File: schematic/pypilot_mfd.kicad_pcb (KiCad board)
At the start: 2 copper layers, 115.8 x 85 mm, 67 parts, among them J1 usb, J2 keypad, J3 Conn_01x02, J4 Conn_01x02, J5 jlx256160, J6 usb, J7 keypad, Q1 Q_PMOS_GSD, Q2 Q_PMOS_GSD, Q3 Q_PMOS_DSG, SW1 BOOT/AP, U1 CH340G, U2 AMS1117-3.3, U3 ESP32-WROOM-32D, U4 BMP280, U5 ADM2587E, U6 LIS2DE12, Y1 12mhz

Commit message: improvements,  ais plotting working
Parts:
- moved J3 1.20 mm to (151.9, 112.8)
- moved J4 1.20 mm to (61.5, 113.0)
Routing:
- net Net-(J1-Pad1): track 49.2 -> 57.0 mm
- net +5V: track 54.4 -> 59.3 mm, vias 2 -> 3
- net TX: track 91.5 -> 87.2 mm
- net +3V3: track 351.9 -> 352.9 mm
- net GND: track 452.8 -> 452.5 mm, vias 11 -> 12
- added copper zone on F.Cu, net +3V3
- added copper zone on B.Cu, net +5V
- added copper zone on B.Cu, net GND
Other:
- outline, holes or cut-outs redrawn

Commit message: update schematic and code fixes
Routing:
- net GND: track 452.5 -> 454.9 mm
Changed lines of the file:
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@@
   (segment (start 73.425 41.775) (end 73.475 42.4875) (width 0.5) (layer F.Cu) (net 1))
   (segment (start 76.325 40.675) (end 75.55 40.575) (width 0.5) (layer F.Cu) (net 1))
-  (segment (start 64.68 32.445) (end 64.68 34.45) (width 0.8) (layer B.Cu) (net 1))
-  (segment (start 65.1 32.025) (end 64.68 32.445) (width 0.8) (layer B.Cu) (net 1))
-  (segment (start 73.475 32.025) (end 65.1 32.025) (width 0.8) (layer B.Cu) (net 1))
-  (segment (start 76.325 40.675) (end 73.475 32.025) (width 0.8) (layer B.Cu) (net 1))
   (segment (start 75.55 40.575) (end 73.425 41.775) (width 0.5) (layer F.Cu) (net 1))
   (via (at 76.325 40.675) (size 0.8) (drill 0.4) (layers F.Cu B.Cu) (net 1))
@@
   (segment (start 72.375 83.65) (end 72.45 83.575) (width 0.4) (layer F.Cu) (net 1))
   (segment (start 72.375 85.375) (end 72.375 83.65) (width 0.4) (layer F.Cu) (net 1))
-  (segment (start 69.6 99.05) (end 69.575 84.475) (width 0.6) (layer B.Cu) (net 1))
-  (segment (start 74.35 101.55) (end 69.6 99.05) (width 0.6) (layer B.Cu) (net 1))
-  (segment (start 90.35 101.8625) (end 74.35 101.55) (width 0.6) (layer B.Cu) (net 1))
+  (segment (start 69.6 100.75) (end 69.575 84.475) (width 0.6) (layer B.Cu) (net 1))
+  (segment (start 70.25 101.75) (end 69.6 100.75) (width 0.6) (layer B.Cu) (net 1))
+  (segment (start 90.35 101.8625) (end 70.25 101.75) (width 0.6) (layer B.Cu) (net 1))
   (segment (start 92.725 98.4) (end 90.35 101.8625) (width 0.6) (layer B.Cu) (net 1))
+  (segment (start 64.68 32.445) (end 64.68 34.45) (width 0.8) (layer B.Cu) (net 1))
+  (segment (start 65.1 32.025) (end 64.68 32.445) (width 0.8) (layer B.Cu) (net 1))
+  (segment (start 74.55 32.025) (end 65.1 32.025) (width 0.8) (layer B.Cu) (net 1))
+  (segment (start 76.325 40.675) (end 74.55 32.025) (width 0.8) (layer B.Cu) (net 1))
   (segment (start 72.475 87.975) (end 78.775 87.975) (width 0.6) (layer F.Cu) (net 2))
   (segment (start 77.6 81.075) (end 76.975 81.075) (width 0.6) (layer F.Cu) (net 2))
@@
   (segment (start 100.425 61.95) (end 90.68 52.205) (width 0.4) (layer F.Cu) (net 11))
   (via (at 118.95 113) (size 0.8) (drill 0.4) (layers F.Cu B.Cu) (net 11))
-  (segment (start 106.025 67.55) (end 100.425 61.95) (width 0.4) (layer B.Cu) (net 11))
-  (segment (start 119.175 87.175) (end 106.025 74.025) (width 0.4) (layer B.Cu) (net 11))
-  (segment (start 106.025 74.025) (end 106.025 67.55) (width 0.4) (layer B.Cu) (net 11))
-  (segment (start 119.15 98.1) (end 119.175 87.175) (width 0.4) (layer B.Cu) (net 11))
-  (segment (start 119 102.05) (end 119.15 98.1) (width 0.4) (layer B.Cu) (net 11))
-  (segment (start 118.95 113) (end 119 102.05) (width 0.4) (layer B.Cu) (net 11))
   (segment (start 107.5 113.1375) (end 107.55 113.1875) (width 0.4) (layer F.Cu) (net 11))
   (segment (start 103.8 113.1375) (end 107.5 113.1375) (width 0.4) (layer F.Cu) (net 11))
   (segment (start 118.7625 113.1875) (end 118.95 113) (width 0.4) (layer F.Cu) (net 11))
   (segment (start 107.55 113.1875) (end 118.7625 113.1875) (width 0.4) (layer F.Cu) (net 11))
+  (segment (start 106.025 74.025) (end 106.025 67.55) (width 0.4) (layer B.Cu) (net 11))
+  (segment (start 119.175 87.175) (end 106.025 74.025) (width 0.4) (layer B.Cu) (net 11))
+  (segment (start 106.025 67.55) (end 100.425 61.95) (width 0.4) (layer B.Cu) (net 11))
+  (segment (start 119.15 98.1) (end 119.175 87.175) (width 0.4) (layer B.Cu) (net 11))
+  (segment (start 119 105) (end 119.15 98.1) (width 0.4) (layer B.Cu) (net 11))
+  (segment (start 118.95 113) (end 119 105) (width 0.4) (layer B.Cu) (net 11))
   (segment (start 118.55 93) (end 119.65 93) (width 0.4) (layer F.Cu) (net 13))
   (segment (start 117.700001 92.150001) (end 118.55 93) (width 0.4) (layer F.Cu) (net 13))
@@
   (segment (start 75.236865 37.580507) (end 74.469831 38.830169) (width 0.4) (layer F.Cu) (net 16))
   (via (at 76.725 35.75) (size 0.8) (drill 0.4) (layers F.Cu B.Cu) (net 16))
-  (segment (start 60.5 38.45) (end 60.5 38.55) (width 0.4) (layer B.Cu) (net 16))
-  (segment (start 61.4 37.55) (end 60.5 38.45) (width 0.4) (layer B.Cu) (net 16))
-  (segment (start 61.4 34.593616) (end 61.4 37.55) (width 0.4) (layer B.Cu) (net 16))
-  (segment (start 62.35 30.85) (end 61.4 34.593616) (width 0.4) (layer B.Cu) (net 16))
-  (segment (start 75.575 30.9) (end 62.35 30.85) (width 0.4) (layer B.Cu) (net 16))
-  (segment (start 76.6 32.7) (end 75.575 30.9) (width 0.4) (layer B.Cu) (net 16))
-  (segment (start 76.725 35.75) (end 76.6 32.7) (width 0.4) (layer B.Cu) (net 16))
   (segment (start 78.8625 38.05) (end 78 38.05) (width 0.25) (layer F.Cu) (net 16))
   (segment (start 76.375 36.425) (end 75.236865 37.580507) (width 0.4) (layer F.Cu) (net 16))
   (segment (start 78 38.05) (end 76.375 36.425) (width 0.25) (layer F.Cu) (net 16))
   (segment (start 76.725 35.75) (end 76.375 36.425) (width 0.4) (layer F.Cu) (net 16))
+  (segment (start 60.5 38.45) (end 60.5 38.55) (width 0.4) (layer B.Cu) (net 16))
+  (segment (start 61.4 34.593616) (end 61.4 37.55) (width 0.4) (layer B.Cu) (net 16))
+  (segment (start 62.35 31) (end 61.4 34.593616) (width 0.4) (layer B.Cu) (net 16))
+  (segment (start 75.55 31) (end 62.35 31) (width 0.4) (layer B.Cu) (net 16))
+  (segment (start 76.6 32.7) (end 75.55 31) (width 0.4) (layer B.Cu) (net 16))
+  (segment (start 61.4 37.55) (end 60.5 38.45) (width 0.4) (layer B.Cu) (net 16))
+  (segment (start 76.725 35.75) (end 76.6 32.7) (width 0.4) (layer B.Cu) (net 16))
   (via (at 84.25 60.925) (size 0.8) (drill 0.4) (layers F.Cu B.Cu) (net 17))
   (segment (start 82.275 60.925) (end 82.105 61.095) (width 0.5) (layer F.Cu) (net 17))
@@
     (polygon
       (pts
-        (xy 84.3 108) (xy 74.95 108) (xy 74.85 84.65) (xy 76.3 83.4) (xy 76.9 79.2)
-        (xy 84.35 80.85)
+        (xy 84.3 108) (xy 60.5 108.25) (xy 74.75 94) (xy 74.85 84.65) (xy 76.3 83.4)
+        (xy 76.9 79.2) (xy 84.25 80)
       )
     )
@@
     (polygon
       (pts
-        (xy 82.5 96.4) (xy 71.25 96.4) (xy 71.25 86.85) (xy 82.5 86.85)
+        (xy 84.25 100) (xy 71.25 100) (xy 71.25 86.85) (xy 84.25 86.85)
       )
     )
@@
     (polygon
       (pts
-        (xy 76.75 79.15) (xy 76.75 85.95) (xy 65.05 85.65) (xy 65.05 79.15)
+        (xy 76.75 79.15) (xy 76.75 85.5) (xy 65.05 85.65) (xy 65.05 79.15)
       )
     )

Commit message: update schematics
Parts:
- removed C9: .1uF, Capacitor_SMD:C_0805_2012Metric
- removed U4: BMP280, pypilot_footprints:Bosch_LGA-8_2x2.5mm_P0.65mm_ClockwisePinNumbering_270
- added R22: 1.2k, Resistor_SMD:R_0805_2012Metric, F.Cu at (148.9, 63.6)
- added R23: 4.7k, Resistor_SMD:R_0805_2012Metric, F.Cu at (137.5, 49.2)
- added R24: 4.7k, Resistor_SMD:R_0805_2012Metric, F.Cu at (135.0, 49.2)
- added R25: 4.7k, Resistor_SMD:R_0805_2012Metric, F.Cu at (132.5, 49.4)
- added R26: 4.7k, Resistor_SMD:R_0805_2012Metric, F.Cu at (124.5, 48.8)
- added U7: 74AHC04, pypilot_footprints:SOT-23-6_180, F.Cu at (153.2, 62.1)
- added U8: BUZZER-freetronics_schematic, pypilot_mfd_footprints:PUIAudio_SMT_0825_S_4_R_90, F.Cu at (153.5, 54.1)
- J2: footprint Connector_PinHeader_2.54mm:PinHeader_1x07_P2.54mm_Vertical -> pypilot_footprints:PinHeader_1x06_P2.54mm_Vertical
- J3, J4: footprint Connector_PinHeader_2.54mm:PinHeader_1x02_P2.54mm_Vertical -> pypilot_mfd_footprints:PinHeader_1x02_P2.54mm_Vertical
- J5: footprint Connector_PinHeader_2.54mm:PinHeader_1x14_P2.54mm_Vertical -> pypilot_mfd_footprints:PinHeader_1x14_P2.54mm_Vertical
- J7: value keypad -> uart
- R12: value 4.7 -> 47
- R19, R20, R8, R9: value 10k -> 1.2k
- R7: value 10k -> 1k
- moved J2 66.6 mm to (131.3, 44.8)
- moved R20 63.7 mm to (137.5, 41.0)
- moved R7 63.7 mm to (127.2, 41.0)
- moved R19 63.7 mm to (135.0, 41.0)
- moved R9 63.6 mm to (132.5, 41.1)
- moved R8 61.8 mm to (124.8, 41.0)
- moved J5 16.7 mm to (104.7, 32.3), turned to 180 degrees
- moved R12 14.0 mm to (111.6, 42.9), turned to 180 degrees
- moved R13 12.8 mm to (110.5, 39.3), turned to 180 degrees
- moved R21 9.45 mm to (114.3, 41.0), turned to 270 degrees
- moved Q3 7.20 mm to (117.3, 41.0), turned to 180 degrees
- moved D2 5.75 mm to (113.3, 112.2)
- moved D3 5.75 mm to (109.5, 112.2)
- moved R17 5.75 mm to (105.0, 112.4)
- turned J3 to 180 degrees
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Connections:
- net Net-(R19-Pad1) renamed MODE
- net Net-(R20-Pad1) renamed DOWN
- net Net-(R9-Pad1) renamed UP
- J2 pad 1: GND -> Net-(J2-Pad1)
- J2 pad 3: Net-(J2-Pad3) -> GND
- R12 pad 2: +3V3 -> +5V
- R7 pad 1: Net-(R7-Pad1) -> PWR_LED
- R8 pad 1: Net-(R8-Pad1) -> PWR
- R8 pad 2: Net-(J2-Pad3) -> Net-(J2-Pad1)
- SW1 pad 1: Net-(SW1-Pad1) -> PWR
- U3 pad 10: Net-(R7-Pad1) -> PWR
- U3 pad 11: Net-(R8-Pad1) -> PWR_LED
- U3 pad 25: Net-(SW1-Pad1) -> PWR
- U3 pad 26: Net-(U3-Pad26) -> BUZZER
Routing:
- net PWR: track 0.00 -> 109.1 mm, vias 0 -> 3
- net BUZZER: track 0.00 -> 81.5 mm, vias 0 -> 2
- net PWR_LED: track 0.00 -> 65.6 mm, vias 0 -> 2
- net +5V: track 59.3 -> 117.7 mm, vias 3 -> 5
- net MODE: track 56.5 -> 105.3 mm
- net Net-(R8-Pad1): track 44.6 -> 0.00 mm
- net Net-(R7-Pad1): track 44.1 -> 0.00 mm
- net DOWN: track 52.2 -> 91.5 mm
- net +3V3: track 352.9 -> 390.9 mm
- net SDA: track 46.7 -> 18.0 mm, vias 2 -> 0
- net UP: track 45.3 -> 69.4 mm, vias 0 -> 2
- net Net-(U7-Pad3): track 0.00 -> 14.9 mm, vias 0 -> 2
- net GND: track 454.9 -> 469.2 mm, vias 12 -> 14
- net SCL: track 40.3 -> 27.6 mm, vias 4 -> 2
- net Net-(SW1-Pad1): track 11.1 -> 0.00 mm, vias 1 -> 0
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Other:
- outline, holes or cut-outs redrawn
- board text added: "pypilot mfd 0.2"

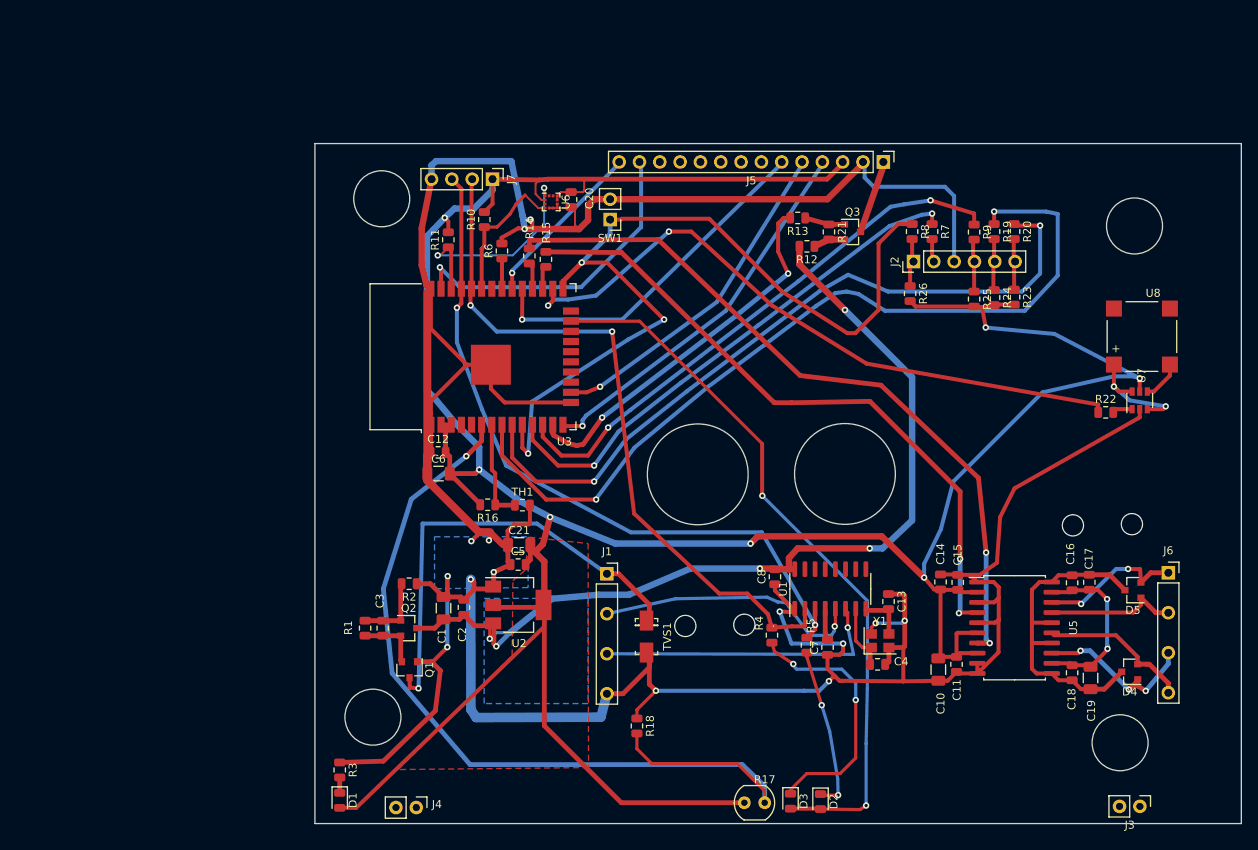
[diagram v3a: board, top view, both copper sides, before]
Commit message: update schematic and enclosure
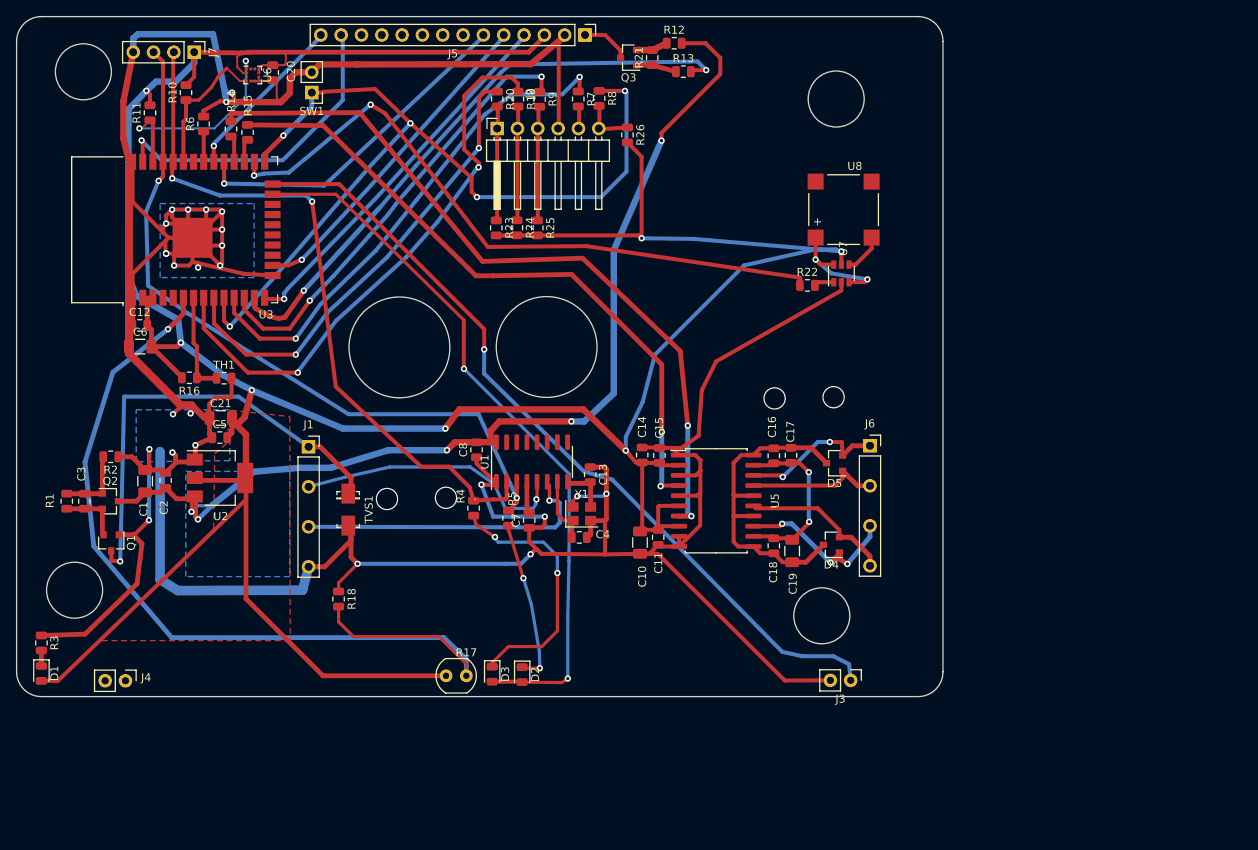
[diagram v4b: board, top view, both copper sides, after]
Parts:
- J2: footprint pypilot_footprints:PinHeader_1x06_P2.54mm_Vertical -> pypilot_mfd_footprints:PinHeader_1x06_P2.54mm_Horizontal
- moved R20 66.7 mm to (72.9, 24.4)
- moved R23 65.3 mm to (72.8, 40.5)
- moved R19 61.8 mm to (75.5, 24.4)
- moved R24 60.3 mm to (75.3, 40.5)
- moved R9 56.8 mm to (78.2, 24.5)
- moved R25 55.3 mm to (77.9, 40.5)
- moved J2 54.6 mm to (79.2, 28.1), turned to 0 degrees
- moved R7 47.2 mm to (83.0, 24.4)
- moved R8 42.5 mm to (85.6, 24.4)
- moved C10 40.5 mm to (90.7, 79.9)
- moved C11 40.5 mm to (93.0, 79.2)
- moved C14 40.5 mm to (91.0, 68.9)
- moved C16 40.5 mm to (107.5, 69.0)
- moved C17 40.5 mm to (109.6, 69.0)
- moved C18 40.5 mm to (107.5, 80.3)
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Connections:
- J2 pad 3: GND -> Net-(J2-Pad3)
- J2 pad 4: Net-(J2-Pad4) -> GND
- J3 pad 2: Net-(J3-Pad2) -> GND
- R19 pad 2: Net-(J2-Pad5) -> Net-(J2-Pad2)
- R20 pad 2: Net-(J2-Pad6) -> Net-(J2-Pad1)
- R23 pad 1: Net-(J2-Pad6) -> Net-(J2-Pad1)
- R24 pad 1: Net-(J2-Pad5) -> Net-(J2-Pad2)
- R25 pad 1: Net-(J2-Pad4) -> Net-(J2-Pad3)
- R26 pad 1: Net-(J2-Pad1) -> Net-(J2-Pad6)
- R7 pad 2: Net-(J2-Pad2) -> Net-(J2-Pad5)
- R8 pad 2: Net-(J2-Pad1) -> Net-(J2-Pad6)
- R9 pad 2: Net-(J2-Pad4) -> Net-(J2-Pad3)
- U3 pad 24: Net-(U3-Pad24) -> Net-(J3-Pad1)
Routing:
- net Net-(J3-Pad1): track 0.00 -> 101.6 mm, vias 0 -> 1
- net GND: track 469.2 -> 554.8 mm, vias 14 -> 26
- net MODE: track 105.3 -> 71.1 mm
- net DOWN: track 91.5 -> 58.5 mm
- net LEDA: track 47.2 -> 74.7 mm
- net +3V3: track 390.9 -> 412.0 mm
- net Net-(J2-Pad3): track 0.00 -> 14.3 mm
- net UP: track 69.4 -> 56.1 mm
- net +5V: track 117.7 -> 129.5 mm
- net Net-(J2-Pad2): track 2.90 -> 14.3 mm
- net Net-(J2-Pad1): track 6.12 -> 14.3 mm
- net Net-(J2-Pad4): track 6.61 -> 0.00 mm
- net Net-(J2-Pad5): track 6.45 -> 2.97 mm
- net Net-(J5-Pad1): track 9.27 -> 6.15 mm
- net TX: track 89.0 -> 91.6 mm
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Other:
- outline, holes or cut-outs redrawn
- board text added: "pypilot mfd 0.3"
- board text removed: "pypilot mfd 0.2"
